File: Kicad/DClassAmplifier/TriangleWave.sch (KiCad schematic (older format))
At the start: 7 parts

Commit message: Finish off Main Part of Schematic
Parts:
- removed R4, R5: 10K, symbol Device:R_Small
- removed U?: TLE2082ACD, D8, symbol 2021-08-03_22-32-07:TLE2082ACD
- added U?: MAX4016ESA+, 21-0041B_8_MXM, symbol MAX4016ESA:MAX4016ESA+
- C1: footprint (none) -> Capacitor_SMD:C_0201_0603Metric_Pad0.64x0.40mm_HandSolder
- R1: value 2.7k -> 2.2k; footprint (none) -> Resistor_SMD:R_0603_1608Metric_Pad0.98x0.95mm_HandSolder
- R2, R3: footprint (none) -> Resistor_SMD:R_0603_1608Metric_Pad0.98x0.95mm_HandSolder
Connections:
- net labels added: VREF
- net labels removed: V_DIVIDER
- wire segments 25 -> 24
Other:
- moved on the sheet: C1
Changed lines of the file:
@@
 $Descr A4 11693 8268
 encoding utf-8
-Sheet 8 9
+Sheet 4 7
 Title ""
 Date ""
@@
 P 5300 2850
 F 0 "R1" V 5104 2850 50  0000 C CNN
-F 1 "2.7k" V 5195 2850 50  0000 C CNN
-F 2 "" H 5300 2850 50  0001 C CNN
+F 1 "2.2k" V 5195 2850 50  0000 C CNN
+F 2 "Resistor_SMD:R_0603_1608Metric_Pad0.98x0.95mm_HandSolder" H 5300 2850 50  0001 C CNN
 F 3 "~" H 5300 2850 50  0001 C CNN
 	1    5300 2850
@@
 $EndComp
 Wire Wire Line
-	5400 2850 6650 2850
-Wire Wire Line
-	6650 2850 6650 3650
+	5400 2850 6600 2850
 Wire Wire Line
 	4100 4100 4100 3750
 $Comp
-L 2021-08-03_22-32-07:TLE2082ACD U?
-U 1 1 6109EC0B
-P 4100 3450
-F 0 "U?" H 5300 3837 60  0000 C CNN
-F 1 "TLE2082ACD" H 5300 3731 60  0000 C CNN
-F 2 "D8" H 5300 3690 60  0001 C CNN
-F 3 "" H 4100 3450 60  0000 C CNN
-	1    4100 3450
-	1    0    0    -1
-$EndComp
-$Comp
 L Device:C_Small C1
 U 1 1 610B0597
-P 7000 3750
-F 0 "C1" H 7092 3796 50  0000 L CNN
-F 1 "10n" H 7092 3705 50  0000 L CNN
-F 2 "" H 7000 3750 50  0001 C CNN
-F 3 "~" H 7000 3750 50  0001 C CNN
-	1    7000 3750
-	1    0    0    -1
+P 6850 3650
+F 0 "C1" V 6950 3575 50  0000 L CNN
+F 1 "10n" V 7025 3575 50  0000 L CNN
+F 2 "Capacitor_SMD:C_0201_0603Metric_Pad0.64x0.40mm_HandSolder" H 6850 3650 50  0001 C CNN
+F 3 "~" H 6850 3650 50  0001 C CNN
+	1    6850 3650
+	0    1    1    0
 $EndComp
-Wire Wire Line
-	6650 3650 6500 3650
-Wire Wire Line
-	6500 3550 7000 3550
 Wire Wire Line
 	7000 3650 7000 3550
@@
 Wire Wire Line
 	7000 3550 7100 3550
-Wire Wire Line
-	6650 3650 6800 3650
-Wire Wire Line
-	6800 3650 6800 3850
-Wire Wire Line
-	6800 3850 7000 3850
-Connection ~ 6650 3650
 $Comp
 L Device:R_Small R2
@@
 F 0 "R2" V 5154 4700 50  0000 C CNN
 F 1 "6k" V 5245 4700 50  0000 C CNN
-F 2 "" H 5350 4700 50  0001 C CNN
+F 2 "Resistor_SMD:R_0603_1608Metric_Pad0.98x0.95mm_HandSolder" H 5350 4700 50  0001 C CNN
 F 3 "~" H 5350 4700 50  0001 C CNN
 	1    5350 4700
@@
 F 0 "R3" H 3559 3596 50  0000 L CNN
 F 1 "27k" H 3559 3505 50  0000 L CNN
-F 2 "" H 3500 3550 50  0001 C CNN
+F 2 "Resistor_SMD:R_0603_1608Metric_Pad0.98x0.95mm_HandSolder" H 3500 3550 50  0001 C CNN
 F 3 "~" H 3500 3550 50  0001 C CNN
 	1    3500 3550
 	1    0    0    -1
 $EndComp
-Text Label 4100 3550 2    50   ~ 0
-V_DIVIDER
-$Comp
-L Device:R_Small R4
-U 1 1 610C0656
-P 2650 3350
-F 0 "R4" H 2709 3396 50  0000 L CNN
-F 1 "10K" H 2709 3305 50  0000 L CNN
-F 2 "" H 2650 3350 50  0001 C CNN
-F 3 "~" H 2650 3350 50  0001 C CNN
-	1    2650 3350
-	1    0    0    -1
-$EndComp
-$Comp
-L Device:R_Small R5
-U 1 1 610C0BDD
-P 2650 3750
-F 0 "R5" H 2709 3796 50  0000 L CNN
-F 1 "10K" H 2709 3705 50  0000 L CNN
-F 2 "" H 2650 3750 50  0001 C CNN
-F 3 "~" H 2650 3750 50  0001 C CNN
-	1    2650 3750
-	1    0    0    -1
-$EndComp
-$Comp
-L power:VCC #PWR?
-U 1 1 610C1135
-P 2650 3250
-F 0 "#PWR?" H 2650 3100 50  0001 C CNN
-F 1 "VCC" H 2665 3423 50  0000 C CNN
-F 2 "" H 2650 3250 50  0001 C CNN
-F 3 "" H 2650 3250 50  0001 C CNN
-	1    2650 3250
-	1    0    0    -1
-$EndComp
-$Comp
-L power:GND #PWR?
-U 1 1 610C18D5
-P 2650 3850
-F 0 "#PWR?" H 2650 3600 50  0001 C CNN
-F 1 "GND" H 2655 3677 50  0000 C CNN
-F 2 "" H 2650 3850 50  0001 C CNN
-F 3 "" H 2650 3850 50  0001 C CNN
-	1    2650 3850
-	1    0    0    -1
-$EndComp
-Wire Wire Line
-	2650 3450 2650 3650
-Text Label 2650 3550 0    50   ~ 0
-V_DIVIDER
 Wire Wire Line
 	3500 3650 3900 3650
@@
 	3900 3650 4100 3650
 Wire Wire Line
-	6650 3650 6650 4700
-Wire Wire Line
 	4100 3550 4000 3550
 Wire Wire Line
@@
 Wire Wire Line
 	6500 4350 6500 3750
+$Comp
+L MAX4016ESA:MAX4016ESA+ U?
+U 1 1 6118D05E
+P 4100 3450
+F 0 "U?" H 5300 3837 60  0000 C CNN
+F 1 "MAX4016ESA+" H 5300 3731 60  0000 C CNN
+F 2 "21-0041B_8_MXM" H 5300 3690 60  0001 C CNN
+F 3 "" H 4100 3450 60  0000 C CNN
+	1    4100 3450
+	1    0    0    -1
+$EndComp
+Text HLabel 4000 3550 0    50   Input ~ 0
+VREF
+Wire Wire Line
+	6950 3650 7000 3650
+Wire Wire Line
+	6500 3650 6600 3650
+Wire Wire Line
+	6500 3550 6650 3550
+Connection ~ 6650 3550
+Wire Wire Line
+	6650 3550 7000 3550
+Wire Wire Line
+	6650 3550 6650 4700
+Wire Wire Line
+	6600 3650 6600 2850
+Connection ~ 6600 3650
+Wire Wire Line
+	6600 3650 6750 3650
 $EndSCHEMATC

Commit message: updates to schematic
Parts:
- added R4: 12k, Resistor_SMD:R_0603_1608Metric_Pad0.98x0.95mm_HandSolder, symbol Device:R_Small
- R2: value 6k -> 12k
- gave numbers to parts that had none: 1
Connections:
- net TRIANGLE_OUT: now also R2.2, R4.2; no longer R2.1
- net at R3.2, U2.3 (INA+): now also R2.1, R4.1; no longer R2.2
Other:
- moved on the sheet: R2
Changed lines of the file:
@@
 $EndDescr
 $Comp
-L power:VCC #PWR?
+L power:VCC #PWR0113
 U 1 1 610A2484
 P 6500 3450
-F 0 "#PWR?" H 6500 3300 50  0001 C CNN
+F 0 "#PWR0113" H 6500 3300 50  0001 C CNN
 F 1 "VCC" H 6515 3623 50  0000 C CNN
 F 2 "" H 6500 3450 50  0001 C CNN
@@
 $EndComp
 $Comp
-L power:GND #PWR?
+L power:GND #PWR0114
 U 1 1 610A5C03
 P 4100 4100
-F 0 "#PWR?" H 4100 3850 50  0001 C CNN
+F 0 "#PWR0114" H 4100 3850 50  0001 C CNN
 F 1 "GND" H 4105 3927 50  0000 C CNN
 F 2 "" H 4100 4100 50  0001 C CNN
@@
 L Device:R_Small R2
 U 1 1 610B770E
-P 5350 4700
-F 0 "R2" V 5154 4700 50  0000 C CNN
-F 1 "6k" V 5245 4700 50  0000 C CNN
-F 2 "Resistor_SMD:R_0603_1608Metric_Pad0.98x0.95mm_HandSolder" H 5350 4700 50  0001 C CNN
-F 3 "~" H 5350 4700 50  0001 C CNN
-	1    5350 4700
-	0    1    1    0
+P 5300 4600
+F 0 "R2" V 5104 4600 50  0000 C CNN
+F 1 "12k" V 5195 4600 50  0000 C CNN
+F 2 "Resistor_SMD:R_0603_1608Metric_Pad0.98x0.95mm_HandSolder" H 5300 4600 50  0001 C CNN
+F 3 "~" H 5300 4600 50  0001 C CNN
+	1    5300 4600
+	0    -1   -1   0
 $EndComp
-Wire Wire Line
-	6650 4700 5450 4700
-Wire Wire Line
-	5250 4700 3900 4700
 Wire Wire Line
 	4100 3450 3900 3450
@@
 Wire Wire Line
 	3500 3650 3900 3650
-Wire Wire Line
-	3900 3650 3900 4700
 Connection ~ 3900 3650
 Wire Wire Line
@@
 	6500 4350 6500 3750
 $Comp
-L MAX4016ESA:MAX4016ESA+ U?
+L MAX4016ESA:MAX4016ESA+ U2
 U 1 1 6118D05E
 P 4100 3450
-F 0 "U?" H 5300 3837 60  0000 C CNN
+F 0 "U2" H 5300 3837 60  0000 C CNN
 F 1 "MAX4016ESA+" H 5300 3731 60  0000 C CNN
 F 2 "21-0041B_8_MXM" H 5300 3690 60  0001 C CNN
@@
 	6650 3550 7000 3550
 Wire Wire Line
-	6650 3550 6650 4700
-Wire Wire Line
 	6600 3650 6600 2850
 Connection ~ 6600 3650
 Wire Wire Line
 	6600 3650 6750 3650
+$Comp
+L Device:R_Small R4
+U 1 1 6110AB92
+P 5300 4950
+F 0 "R4" V 5104 4950 50  0000 C CNN
+F 1 "12k" V 5195 4950 50  0000 C CNN
+F 2 "Resistor_SMD:R_0603_1608Metric_Pad0.98x0.95mm_HandSolder" H 5300 4950 50  0001 C CNN
+F 3 "~" H 5300 4950 50  0001 C CNN
+	1    5300 4950
+	0    -1   -1   0
+$EndComp
+Wire Wire Line
+	5200 4600 5050 4600
+Wire Wire Line
+	5050 4600 5050 4750
+Wire Wire Line
+	5050 4950 5200 4950
+Wire Wire Line
+	5400 4950 5550 4950
+Wire Wire Line
+	5550 4950 5550 4750
+Wire Wire Line
+	5550 4600 5400 4600
+Wire Wire Line
+	6650 4750 5550 4750
+Wire Wire Line
+	6650 3550 6650 4750
+Connection ~ 5550 4750
+Wire Wire Line
+	5550 4750 5550 4600
+Wire Wire Line
+	5050 4750 3900 4750
+Wire Wire Line
+	3900 3650 3900 4750
+Connection ~ 5050 4750
+Wire Wire Line
+	5050 4750 5050 4950
 $EndSCHEMATC

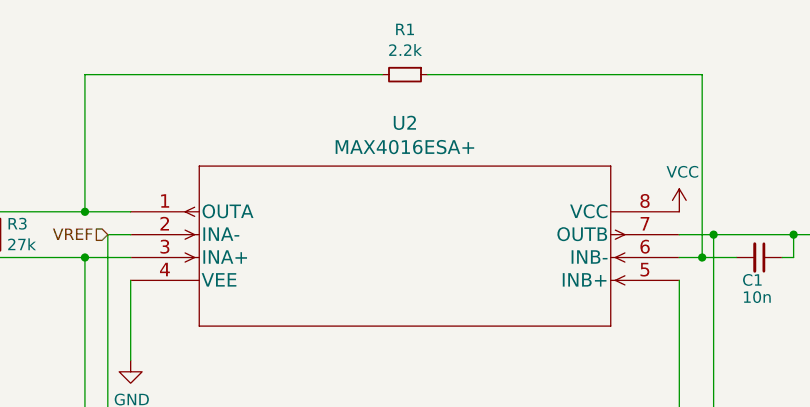
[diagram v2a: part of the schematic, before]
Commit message: Update Opamp for Input Filter
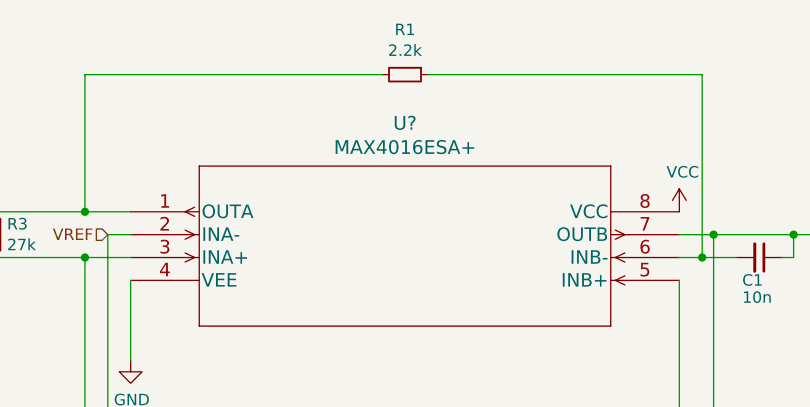
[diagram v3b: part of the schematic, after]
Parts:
- removed U2: MAX4016ESA+, 21-0041B_8_MXM, symbol MAX4016ESA:MAX4016ESA+
- added U?: MAX4016ESA+, 21-0041B_8_MXM, symbol MAX4016ESA:MAX4016ESA+
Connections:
- net GND: now also U?.4 (VEE)
- net TRIANGLE_OUT: now also U?.7 (OUTB)
- net VCC: now also U?.8 (VCC)
- net VREF: now also U?.2 (INA-), U?.5 (INB+)
- net at C1.2, R1.1: now also U?.6 (INB-)
- net at R1.2, R3.1: now also U?.1 (OUTA)
- net at R2.1, R3.2, R4.1: now also U?.3 (INA+)
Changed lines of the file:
@@
 $Descr A4 11693 8268
 encoding utf-8
-Sheet 4 7
+Sheet 4 6
 Title ""
 Date ""
@@
 Wire Wire Line
 	6500 4350 6500 3750
-$Comp
-L MAX4016ESA:MAX4016ESA+ U2
-U 1 1 6118D05E
-P 4100 3450
-F 0 "U2" H 5300 3837 60  0000 C CNN
-F 1 "MAX4016ESA+" H 5300 3731 60  0000 C CNN
-F 2 "21-0041B_8_MXM" H 5300 3690 60  0001 C CNN
-F 3 "" H 4100 3450 60  0000 C CNN
-	1    4100 3450
-	1    0    0    -1
-$EndComp
 Text HLabel 4000 3550 0    50   Input ~ 0
 VREF
@@
 Wire Wire Line
 	5050 4750 5050 4950
+$Comp
+L MAX4016ESA:MAX4016ESA+ U?
+U 1 1 610FB9E0
+P 4100 3450
+F 0 "U?" H 5300 3837 60  0000 C CNN
+F 1 "MAX4016ESA+" H 5300 3731 60  0000 C CNN
+F 2 "21-0041B_8_MXM" H 5300 3690 60  0001 C CNN
+F 3 "" H 4100 3450 60  0000 C CNN
+	1    4100 3450
+	1    0    0    -1
+$EndComp
 $EndSCHEMATC

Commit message: Added footprints to schematic
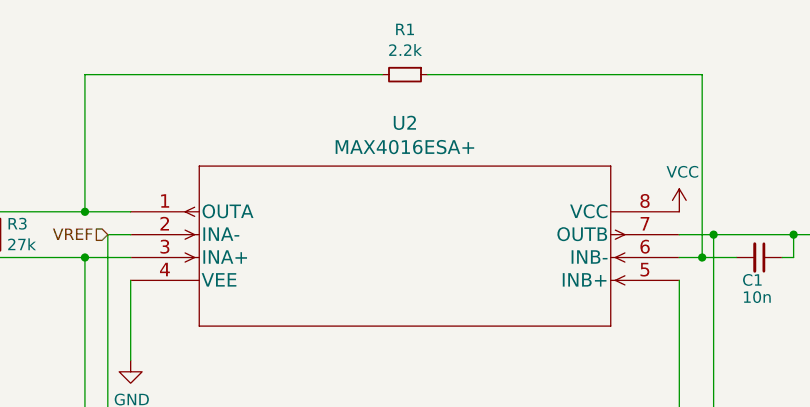
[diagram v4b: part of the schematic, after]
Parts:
- gave numbers to parts that had none: 1
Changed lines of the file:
@@
 	5050 4750 5050 4950
 $Comp
-L MAX4016ESA:MAX4016ESA+ U?
+L MAX4016ESA:MAX4016ESA+ U2
 U 1 1 610FB9E0
 P 4100 3450
-F 0 "U?" H 5300 3837 60  0000 C CNN
+F 0 "U2" H 5300 3837 60  0000 C CNN
 F 1 "MAX4016ESA+" H 5300 3731 60  0000 C CNN
 F 2 "21-0041B_8_MXM" H 5300 3690 60  0001 C CNN

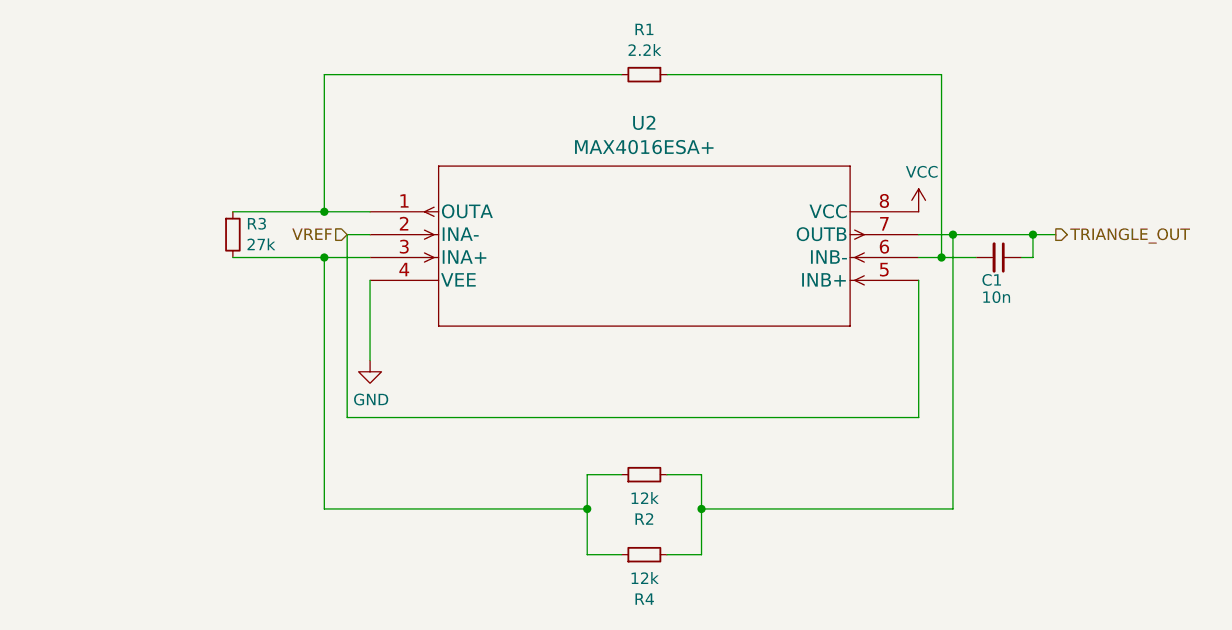
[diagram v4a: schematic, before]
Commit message: Add Test Points
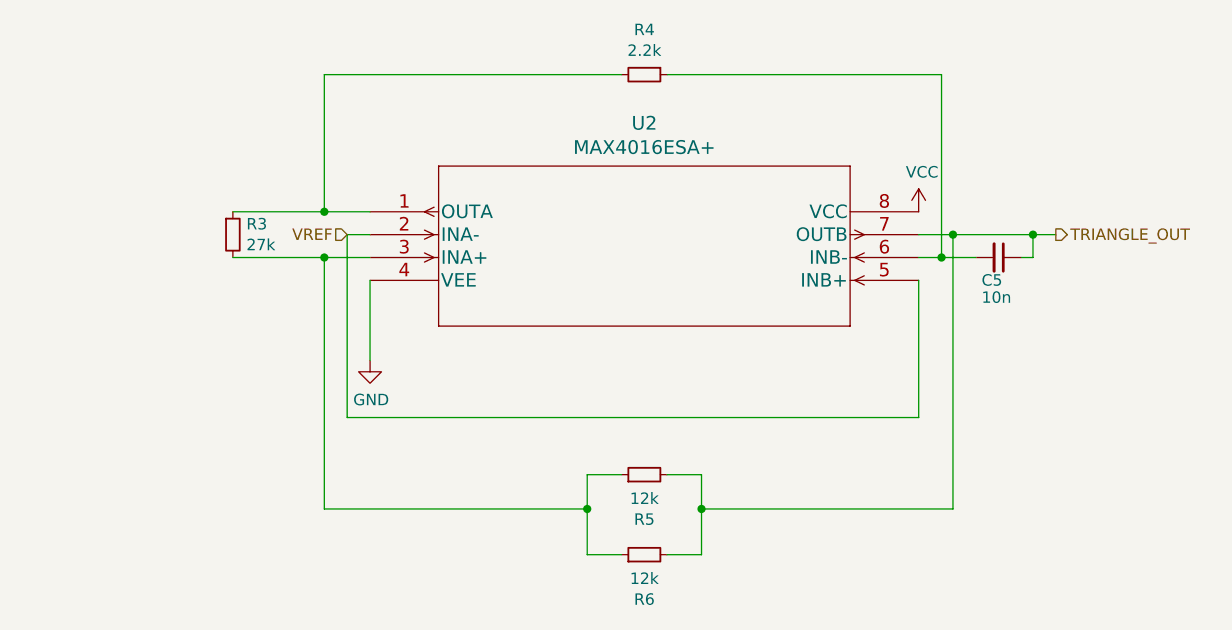
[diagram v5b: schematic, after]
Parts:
- renumbered C1 to C5, R1 to R4, R2 to R5, R4 to R6
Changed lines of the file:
@@
 $EndDescr
 $Comp
-L power:VCC #PWR0113
+L power:VCC #PWR015
 U 1 1 610A2484
 P 6500 3450
-F 0 "#PWR0113" H 6500 3300 50  0001 C CNN
+F 0 "#PWR015" H 6500 3300 50  0001 C CNN
 F 1 "VCC" H 6515 3623 50  0000 C CNN
 F 2 "" H 6500 3450 50  0001 C CNN
@@
 $EndComp
 $Comp
-L power:GND #PWR0114
+L power:GND #PWR014
 U 1 1 610A5C03
 P 4100 4100
-F 0 "#PWR0114" H 4100 3850 50  0001 C CNN
+F 0 "#PWR014" H 4100 3850 50  0001 C CNN
 F 1 "GND" H 4105 3927 50  0000 C CNN
 F 2 "" H 4100 4100 50  0001 C CNN
@@
 TRIANGLE_OUT
 $Comp
-L Device:R_Small R1
+L Device:R_Small R4
 U 1 1 610ABFC7
 P 5300 2850
-F 0 "R1" V 5104 2850 50  0000 C CNN
+F 0 "R4" V 5104 2850 50  0000 C CNN
 F 1 "2.2k" V 5195 2850 50  0000 C CNN
 F 2 "Resistor_SMD:R_0603_1608Metric_Pad0.98x0.95mm_HandSolder" H 5300 2850 50  0001 C CNN
@@
 	4100 4100 4100 3750
 $Comp
-L Device:C_Small C1
+L Device:C_Small C5
 U 1 1 610B0597
 P 6850 3650
-F 0 "C1" V 6950 3575 50  0000 L CNN
+F 0 "C5" V 6950 3575 50  0000 L CNN
 F 1 "10n" V 7025 3575 50  0000 L CNN
 F 2 "Capacitor_SMD:C_0201_0603Metric_Pad0.64x0.40mm_HandSolder" H 6850 3650 50  0001 C CNN
@@
 	7000 3550 7100 3550
 $Comp
-L Device:R_Small R2
+L Device:R_Small R5
 U 1 1 610B770E
 P 5300 4600
-F 0 "R2" V 5104 4600 50  0000 C CNN
+F 0 "R5" V 5104 4600 50  0000 C CNN
 F 1 "12k" V 5195 4600 50  0000 C CNN
 F 2 "Resistor_SMD:R_0603_1608Metric_Pad0.98x0.95mm_HandSolder" H 5300 4600 50  0001 C CNN
@@
 	6600 3650 6750 3650
 $Comp
-L Device:R_Small R4
+L Device:R_Small R6
 U 1 1 6110AB92
 P 5300 4950
-F 0 "R4" V 5104 4950 50  0000 C CNN
+F 0 "R6" V 5104 4950 50  0000 C CNN
 F 1 "12k" V 5195 4950 50  0000 C CNN
 F 2 "Resistor_SMD:R_0603_1608Metric_Pad0.98x0.95mm_HandSolder" H 5300 4950 50  0001 C CNN

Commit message: Load Components into PCBDOC
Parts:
- U2: footprint 21-0041B_8_MXM -> MAX4016ESA:MAX4016ESA&plus_
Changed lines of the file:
@@
 F 0 "U2" H 5300 3837 60  0000 C CNN
 F 1 "MAX4016ESA+" H 5300 3731 60  0000 C CNN
-F 2 "21-0041B_8_MXM" H 5300 3690 60  0001 C CNN
+F 2 "MAX4016ESA:MAX4016ESA&plus_" H 5300 3690 60  0001 C CNN
 F 3 "" H 4100 3450 60  0000 C CNN
 	1    4100 3450

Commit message: Added input to global schematic
Changed the sig_in net label in the LPF sheet to a hierarchical net label of the same name
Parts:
- U2: symbol MAX4016ESA:MAX4016ESA+ -> DClassAmplifier-rescue:MAX4016ESA+-MAX4016ESA
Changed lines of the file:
@@
 	5050 4750 5050 4950
 $Comp
-L MAX4016ESA:MAX4016ESA+ U2
+L DClassAmplifier-rescue:MAX4016ESA+-MAX4016ESA U2
 U 1 1 610FB9E0
 P 4100 3450

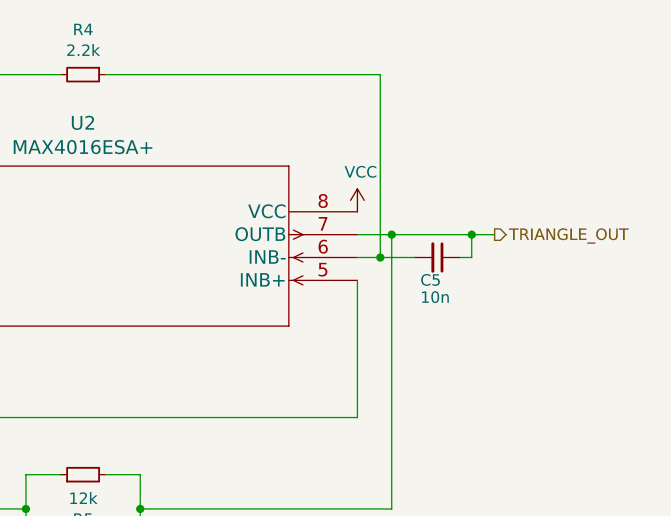
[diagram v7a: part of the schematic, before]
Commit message: PCB for input and added filter caps
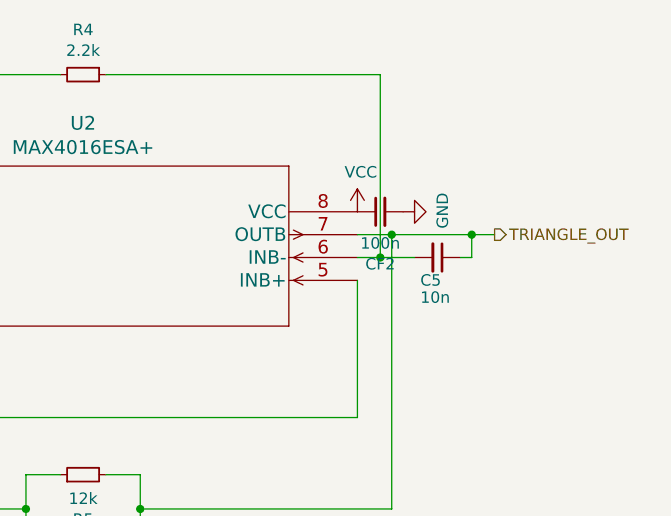
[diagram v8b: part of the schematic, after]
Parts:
- added CF2: 100n, Capacitor_SMD:C_0805_2012Metric_Pad1.18x1.45mm_HandSolder, symbol Device:C_Small
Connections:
- net GND: now also CF2.2
- net VCC: now also CF2.1
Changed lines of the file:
@@
 	1    0    0    -1
 $EndComp
+$Comp
+L Device:C_Small CF?
+U 1 1 611DAEFE
+P 6600 3450
+AR Path="/610C616D/611DAEFE" Ref="CF?"  Part="1"
+AR Path="/611D4178/611DAEFE" Ref="CF?"  Part="1"
+AR Path="/6109BB03/611DAEFE" Ref="CF2"  Part="1"
+F 0 "CF2" V 6371 3450 50  0000 C CNN
+F 1 "100n" V 6462 3450 50  0000 C CNN
+F 2 "Capacitor_SMD:C_0805_2012Metric_Pad1.18x1.45mm_HandSolder" H 6600 3450 50  0001 C CNN
+F 3 "~" H 6600 3450 50  0001 C CNN
+	1    6600 3450
+	0    -1   -1   0
+$EndComp
+$Comp
+L power:GND #PWR?
+U 1 1 611DAF04
+P 6700 3450
+F 0 "#PWR?" H 6700 3200 50  0001 C CNN
+F 1 "GND" H 6705 3277 50  0000 C CNN
+F 2 "" H 6700 3450 50  0001 C CNN
+F 3 "" H 6700 3450 50  0001 C CNN
+	1    6700 3450
+	0    -1   -1   0
+$EndComp
 $EndSCHEMATC
